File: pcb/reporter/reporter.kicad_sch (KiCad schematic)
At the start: 41 parts, among them J1 BOOT_MODE, J2 USB_B_Micro, J3 BATTERY, Q1 Q_Photo_NPN, SW1 RESET, SW2 BAT_EN, U1 ESP32-C3-WROOM-02, U2 MAX40200AUK, U3 MCP73831-2-OT, U4 LD39150DT33

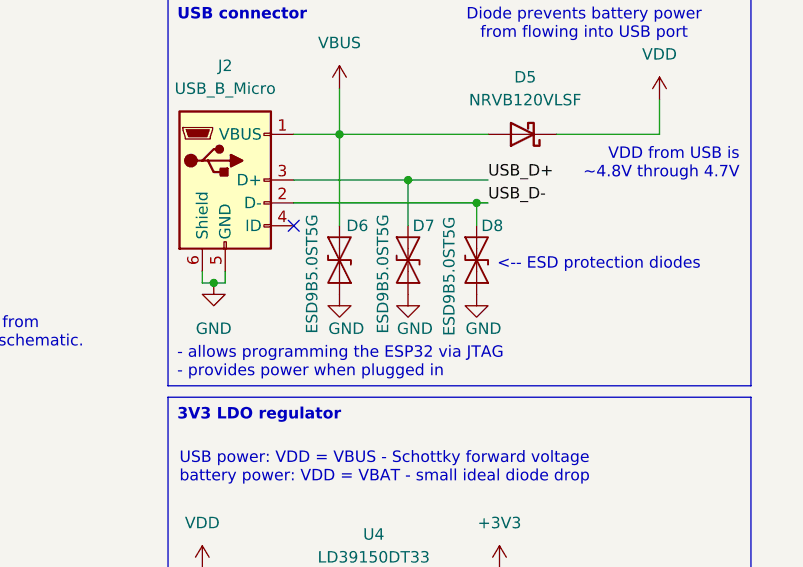
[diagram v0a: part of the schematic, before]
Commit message: replace ESD diodes with larger package
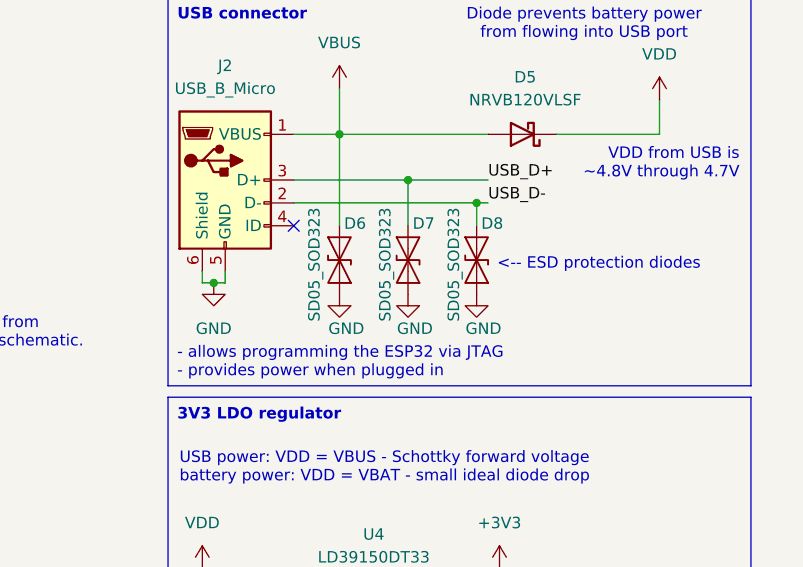
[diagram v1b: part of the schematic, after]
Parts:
- removed D6, D7, D8: ESD9B5.0ST5G, Diode_SMD:D_SOD-923, symbol Diode:ESD9B5.0ST5G
- added D6, D7, D8: SD05_SOD323, Diode_SMD:D_SOD-323, symbol Diode:SD05_SOD323
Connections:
- net GND: now also D6.2 (A2), D7.2 (A2), D8.2 (A2)
- net USB_D+: now also D7.1 (A1)
- net USB_D-: now also D8.1 (A1)
- net VBUS: now also D6.1 (A1)
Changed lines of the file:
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@@
 	)
 	(symbol
+		(lib_id "Diode:SD05_SOD323")
+		(at 219.71 54.61 270)
+		(unit 1)
+		(exclude_from_sim no)
+		(in_bom yes)
+		(on_board yes)
+		(dnp no)
+		(property "Reference" "D6"
+			(at 220.218 50.546 90)
+			(effects
+				(font
+					(size 1.27 1.27)
+				)
+				(justify left)
+			)
+		)
+		(property "Value" "SD05_SOD323"
+			(at 216.916 48.768 0)
+			(effects
+				(font
+					(size 1.27 1.27)
+				)
+				(justify left)
+			)
+		)
+		(property "Footprint" "Diode_SMD:D_SOD-323"
+			(at 214.63 54.61 0)
+			(effects
+				(font
+					(size 1.27 1.27)
+				)
+				(hide yes)
+			)
+		)
+		(property "Datasheet" "https://www.diodes.com/assets/Datasheets/SD05C.pdf"
+			(at 219.71 54.61 0)
+			(effects
+				(font
+					(size 1.27 1.27)
+				)
+				(hide yes)
+			)
+		)
+		(property "Description" "5V, 450W Discrete Bidirectional TVS Diode, SOD-323"
+			(at 219.71 54.61 0)
+			(effects
+				(font
+					(size 1.27 1.27)
+				)
+				(hide yes)
+			)
+		)
+		(property "Part Number" "SD05C-7"
+			(at 219.71 54.61 0)
+			(effects
+				(font
+					(size 1.27 1.27)
+				)
+				(hide yes)
+			)
+		)
+		(pin "1"
+		)
+		(pin "2"
+		)
+		(instances
+			(project "reporter"
+				(path "/1f39f509-fadf-4ef8-8f0f-fb272e08b99c"
+					(reference "D6")
+					(unit 1)
+				)
+			)
+		)
+	)
+	(symbol
 		(lib_id "power:GND")
 		(at 63.5 162.56 0)
@@
 	)
 	(symbol
-		(lib_id "Diode:ESD9B5.0ST5G")
-		(at 234.95 54.61 90)
+		(lib_id "Diode:SD05_SOD323")
+		(at 234.95 54.61 270)
 		(unit 1)
 		(exclude_from_sim no)
@@
 		(dnp no)
 		(property "Reference" "D8"
-			(at 235.458 50.8 90)
+			(at 235.458 50.546 90)
 			(effects
 				(font
 					(size 1.27 1.27)
 				)
-				(justify right)
+				(justify left)
 			)
 		)
-		(property "Value" "ESD9B5.0ST5G"
-			(at 231.902 49.784 0)
+		(property "Value" "SD05_SOD323"
+			(at 232.41 48.768 0)
 			(effects
 				(font
 					(size 1.27 1.27)
 				)
-				(justify right)
+				(justify left)
 			)
 		)
-		(property "Footprint" "Diode_SMD:D_SOD-923"
-			(at 234.95 54.61 0)
+		(property "Footprint" "Diode_SMD:D_SOD-323"
+			(at 229.87 54.61 0)
 			(effects
 				(font
@@
 			)
 		)
-		(property "Datasheet" "https://www.onsemi.com/pub/Collateral/ESD9B-D.PDF"
+		(property "Datasheet" "https://www.diodes.com/assets/Datasheets/SD05C.pdf"
 			(at 234.95 54.61 0)
 			(effects
@@
 			)
 		)
-		(property "Description" "ESD protection diode, 5.0Vrwm, SOD-923"
+		(property "Description" "5V, 450W Discrete Bidirectional TVS Diode, SOD-323"
 			(at 234.95 54.61 0)
 			(effects
@@
 			)
 		)
-		(property "Part Number" "ESD9B5.0ST5G"
+		(property "Part Number" "SD05C-7"
 			(at 234.95 54.61 0)
 			(effects
@@
 			)
 		)
-		(pin "2"
-		)
 		(pin "1"
 		)
+		(pin "2"
+		)
 		(instances
 			(project "reporter"
@@
 	)
 	(symbol
-		(lib_id "Diode:ESD9B5.0ST5G")
-		(at 227.33 54.61 90)
-		(unit 1)
-		(exclude_from_sim no)
-		(in_bom yes)
-		(on_board yes)
-		(dnp no)
-		(property "Reference" "D7"
-			(at 227.838 50.8 90)
-			(effects
-				(font
-					(size 1.27 1.27)
-				)
-				(justify right)
-			)
-		)
-		(property "Value" "ESD9B5.0ST5G"
-			(at 224.536 49.53 0)
-			(effects
-				(font
-					(size 1.27 1.27)
-				)
-				(justify right)
-			)
-		)
-		(property "Footprint" "Diode_SMD:D_SOD-923"
-			(at 227.33 54.61 0)
-			(effects
-				(font
-					(size 1.27 1.27)
-				)
-				(hide yes)
-			)
-		)
-		(property "Datasheet" "https://www.onsemi.com/pub/Collateral/ESD9B-D.PDF"
-			(at 227.33 54.61 0)
-			(effects
-				(font
-					(size 1.27 1.27)
-				)
-				(hide yes)
-			)
-		)
-		(property "Description" "ESD protection diode, 5.0Vrwm, SOD-923"
-			(at 227.33 54.61 0)
-			(effects
-				(font
-					(size 1.27 1.27)
-				)
-				(hide yes)
-			)
-		)
-		(property "Part Number" "ESD9B5.0ST5G"
-			(at 227.33 54.61 0)
-			(effects
-				(font
-					(size 1.27 1.27)
-				)
-				(hide yes)
-			)
-		)
-		(pin "2"
-		)
-		(pin "1"
-		)
-		(instances
-			(project "reporter"
-				(path "/1f39f509-fadf-4ef8-8f0f-fb272e08b99c"
-					(reference "D7")
-					(unit 1)
-				)
-			)
-		)
-	)
-	(symbol
 		(lib_id "power:GND")
 		(at 203.2 157.48 0)
@@
 	)
 	(symbol
-		(lib_id "Diode:ESD9B5.0ST5G")
-		(at 219.71 54.61 90)
-		(unit 1)
-		(exclude_from_sim no)
-		(in_bom yes)
-		(on_board yes)
-		(dnp no)
-		(property "Reference" "D6"
-			(at 220.472 50.8 90)
-			(effects
-				(font
-					(size 1.27 1.27)
-				)
-				(justify right)
-			)
-		)
-		(property "Value" "ESD9B5.0ST5G"
-			(at 216.662 49.53 0)
-			(effects
-				(font
-					(size 1.27 1.27)
-				)
-				(justify right)
-			)
-		)
-		(property "Footprint" "Diode_SMD:D_SOD-923"
-			(at 219.71 54.61 0)
-			(effects
-				(font
-					(size 1.27 1.27)
-				)
-				(hide yes)
-			)
-		)
-		(property "Datasheet" "https://www.onsemi.com/pub/Collateral/ESD9B-D.PDF"
-			(at 219.71 54.61 0)
-			(effects
-				(font
-					(size 1.27 1.27)
-				)
-				(hide yes)
-			)
-		)
-		(property "Description" "ESD protection diode, 5.0Vrwm, SOD-923"
-			(at 219.71 54.61 0)
-			(effects
-				(font
-					(size 1.27 1.27)
-				)
-				(hide yes)
-			)
-		)
-		(property "Part Number" "ESD9B5.0ST5G"
-			(at 219.71 54.61 0)
-			(effects
-				(font
-					(size 1.27 1.27)
-				)
-				(hide yes)
-			)
-		)
-		(pin "2"
-		)
-		(pin "1"
-		)
-		(instances
-			(project "reporter"
-				(path "/1f39f509-fadf-4ef8-8f0f-fb272e08b99c"
-					(reference "D6")
-					(unit 1)
-				)
-			)
-		)
-	)
-	(symbol
 		(lib_id "Device:C_Small")
 		(at 83.82 190.5 270)
@@
 					(unit 1)
 				)
+			)
+		)
+	)
+	(symbol
+		(lib_id "Diode:SD05_SOD323")
+		(at 227.33 54.61 270)
+		(unit 1)
+		(exclude_from_sim no)
+		(in_bom yes)
+		(on_board yes)
+		(dnp no)
+		(property "Reference" "D7"
+			(at 227.838 50.546 90)
+			(effects
+				(font
+					(size 1.27 1.27)
+				)
+				(justify left)
+			)
+		)
+		(property "Value" "SD05_SOD323"
+			(at 224.79 48.768 0)
+			(effects
+				(font
+					(size 1.27 1.27)
+				)
+				(justify left)
+			)
+		)
+		(property "Footprint" "Diode_SMD:D_SOD-323"
+			(at 222.25 54.61 0)
+			(effects
+				(font
+					(size 1.27 1.27)
+				)
+				(hide yes)
+			)
+		)
+		(property "Datasheet" "https://www.diodes.com/assets/Datasheets/SD05C.pdf"
+			(at 227.33 54.61 0)
+			(effects
+				(font
+					(size 1.27 1.27)
+				)
+				(hide yes)
+			)
+		)
+		(property "Description" "5V, 450W Discrete Bidirectional TVS Diode, SOD-323"
+			(at 227.33 54.61 0)
+			(effects
+				(font
+					(size 1.27 1.27)
+				)
+				(hide yes)
+			)
+		)
+		(property "Part Number" "SD05C-7"
+			(at 227.33 54.61 0)
+			(effects
+				(font
+					(size 1.27 1.27)
+				)
+				(hide yes)
+			)
+		)
+		(pin "1"
+		)
+		(pin "2"
+		)
+		(instances
+			(project "reporter"
+				(path "/1f39f509-fadf-4ef8-8f0f-fb272e08b99c"
+					(reference "D7")
+					(unit 1)
+				)

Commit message: use USB connector with board guides
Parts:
- J2: footprint Connector_USB:USB_Micro-B_Amphenol_10118193-0001LF_Horizontal -> Connector_USB:USB_Micro-B_Wuerth_629105150521; Part Number 10118193-0001LF -> 629105150521
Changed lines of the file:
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@@
 			)
 		)
-		(property "Footprint" "Connector_USB:USB_Micro-B_Amphenol_10118193-0001LF_Horizontal"
+		(property "Footprint" "Connector_USB:USB_Micro-B_Wuerth_629105150521"
 			(at 210.82 46.99 0)
 			(effects
@@
 			)
 		)
-		(property "Datasheet" "https://cdn.amphenol-cs.com/media/wysiwyg/files/documentation/datasheet/inputoutput/io_usb_micro.pdf"
+		(property "Datasheet" "https://www.we-online.com/katalog/datasheet/629105150521.pdf"
 			(at 210.82 46.99 0)
 			(effects
@@
 			)
 		)
-		(property "Part Number" "10118193-0001LF"
+		(property "Part Number" "629105150521"
 			(at 207.01 45.72 0)
 			(effects
